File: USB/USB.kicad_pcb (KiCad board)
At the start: 4 copper layers, 70 x 60 mm, 20 parts, among them J1 USBC-4-0-CX90MW9-24P1, U2 ESDA25L, U3 USB SWITCH 2CHANNEL TS3USB221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, U6 usb-polarity-TUSB321RWBR

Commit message: added TVS protection and filtering to CC lines
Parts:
- added TVS4: ~, SPIRIT-footprints:1-channel-TVS-choke-XDFN6_1P2X1P2_ONS, F.Cu at (116.6, 82.4)
- moved J2 0.60 mm to (111.9, 83.7)
- moved J3 0.53 mm to (109.4, 83.7)
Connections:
- J1 pad A1: GND -> Net-(J1-GND_A)
- J1 pad A12: GND -> Net-(J1-GND_A)
- J2 pad 1: CC1 -> CC1f
- J2 pad 2: Net-(U6-CC1) -> CC1f-jumpered
- J3 pad 1: CC2 -> CC2f
- J3 pad 2: Net-(U6-CC2) -> CC2f-jumpered
- Module1 pad 94: CC1 -> CC1f-jumpered
- Module1 pad 96: CC2 -> CC2f-jumpered
- U6 pad 1: Net-(U6-CC1) -> CC1f-jumpered
- U6 pad 2: Net-(U6-CC2) -> CC2f-jumpered
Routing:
- net CC1f-jumpered: track 0.00 -> 57.0 mm, vias 0 -> 2
- net CC2f-jumpered: track 0.00 -> 56.3 mm, vias 0 -> 2
- net CC2: track 25.8 -> 16.8 mm
- net Net-(U6-CC1): track 8.32 -> 0.00 mm
- net Net-(U6-CC2): track 8.21 -> 0.00 mm
- net CC2f: track 0.00 -> 7.82 mm
- net CC1f: track 0.00 -> 4.58 mm
- net CC1: track 16.5 -> 12.7 mm

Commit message: fix TVS protection on CC lines
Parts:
- removed TVS4: ~, SPIRIT-footprints:1-channel-TVS-choke-XDFN6_1P2X1P2_ONS
- added D1: TPD1E05U06DPYR, CM5IO:TPD1E05U-SON65P60X100X45-2N, F.Cu at (120.8, 87.0)
- added D2: TPD1E05U06DPYR, CM5IO:TPD1E05U-SON65P60X100X45-2N, F.Cu at (122.8, 85.6)
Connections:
- net CC1f-jumpered renamed CC1-jumpered
- J2 pad 1: CC1f -> CC1
- J3 pad 1: CC2f -> CC2
- J3 pad 2: CC2f-jumpered -> CC2-jumpered
- Module1 pad 96: CC2f-jumpered -> CC2n-jumpered
- U6 pad 2: CC2f-jumpered -> CC2-jumpered
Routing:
- net CC2f-jumpered: track 56.3 -> 0.00 mm, vias 2 -> 0
- net (no net): track 0.00 -> 56.3 mm, vias 0 -> 2
- net CC2: track 16.8 -> 25.5 mm
- net CC2f: track 7.82 -> 0.00 mm
- net CC1f: track 4.58 -> 0.00 mm
- net CC1: track 12.7 -> 17.3 mm

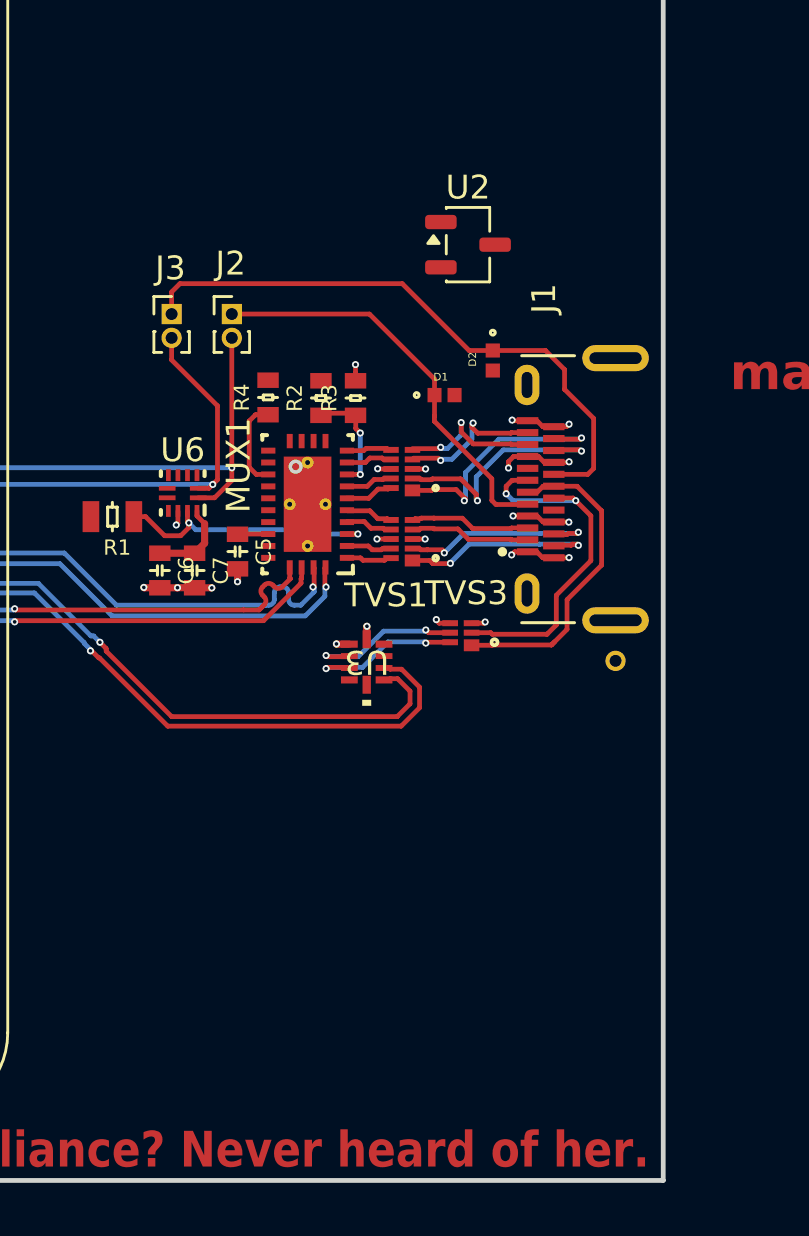
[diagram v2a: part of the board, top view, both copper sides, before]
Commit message: add lab power input headers
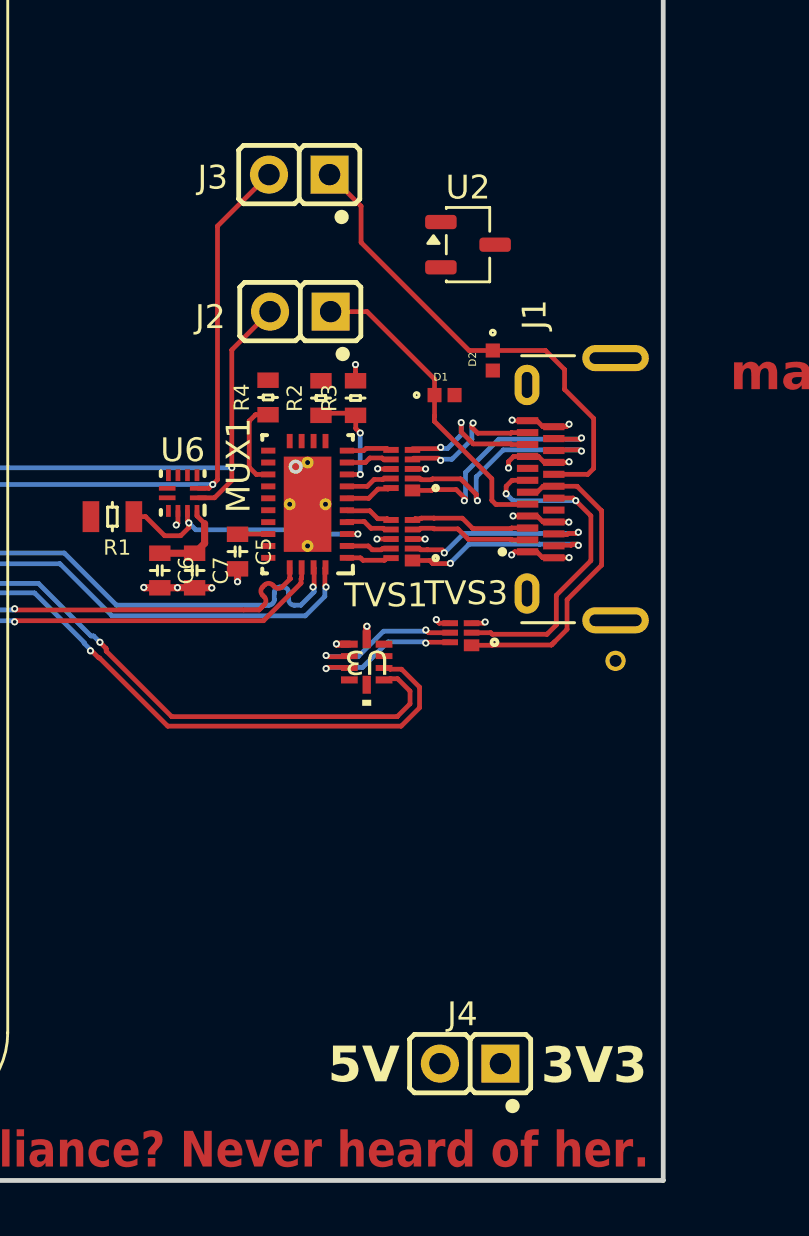
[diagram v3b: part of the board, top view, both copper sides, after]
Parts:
- added J4: ~, COMATEL THD:COMATEL_385.0358.1.02.400, F.Cu at (123.2, 115.1)
- J2, J3: footprint Connector_PinHeader_1.00mm:PinHeader_1x02_P1.00mm_Vertical -> COMATEL THD:COMATEL_385.0358.1.02.400
- moved J3 8.84 mm to (116.0, 77.8), turned to 180 degrees
- moved J2 4.15 mm to (116.0, 83.5), turned to 180 degrees
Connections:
- Module1 pad 96: CC2n-jumpered -> CC2-jumpered
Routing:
- net CC2-jumpered: track 0.00 -> 63.3 mm, vias 0 -> 2
- net (no net): track 56.3 -> 0.00 mm, vias 2 -> 0
- net CC2: track 25.5 -> 20.6 mm
- net CC1: track 17.3 -> 13.2 mm
- net CC1-jumpered: track 57.0 -> 58.8 mm
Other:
- board text added: "3V3"
- board text added: "5V"

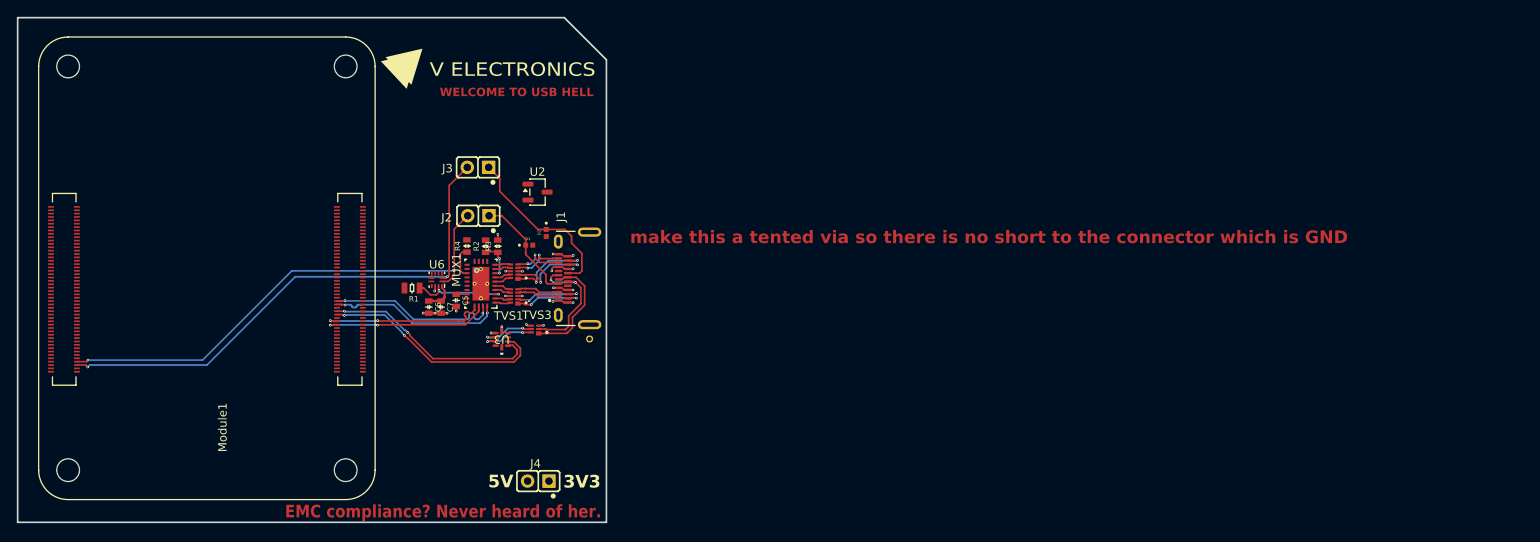
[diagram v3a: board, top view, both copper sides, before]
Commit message: add copper pours
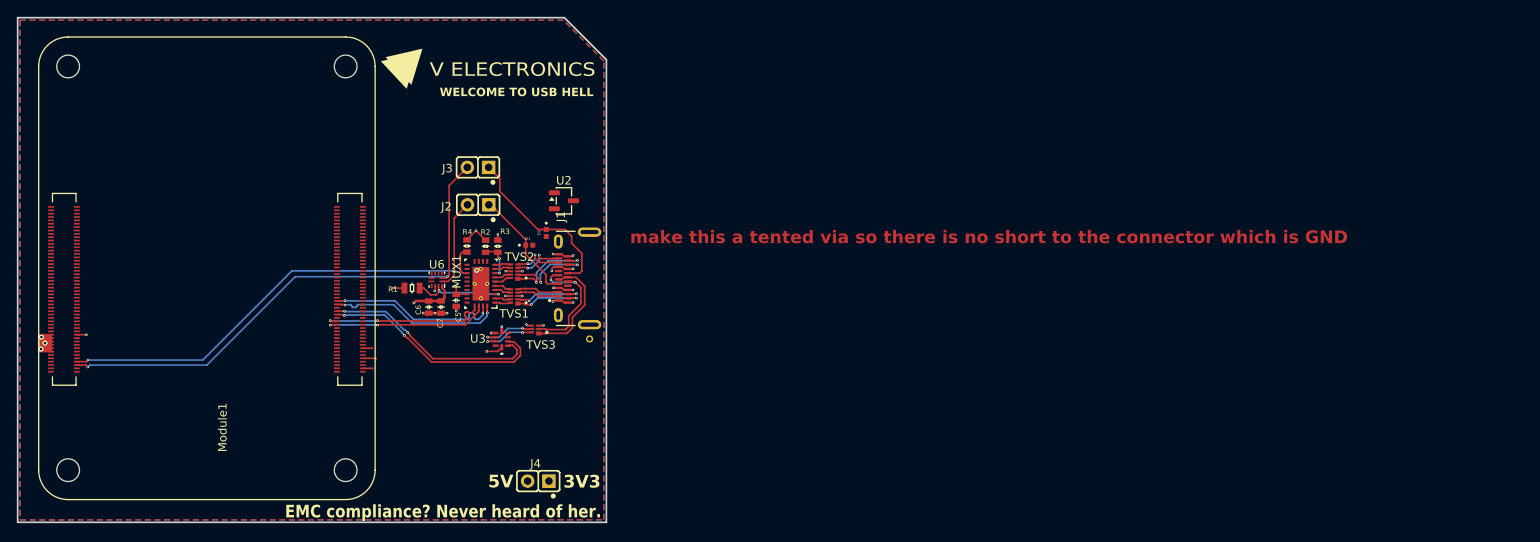
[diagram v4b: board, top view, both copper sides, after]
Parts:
- moved U2 3.31 mm to (125.0, 81.8)
- moved J2 1.30 mm to (116.0, 82.2)
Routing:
- net 3V3B: track 1.29 -> 9.87 mm, vias 0 -> 5
- net GND: track 14.4 -> 18.3 mm
- net 5V: track 3.54 -> 5.42 mm, vias 0 -> 4
- net CC1-jumpered: track 58.8 -> 60.1 mm
- net CC1: track 13.2 -> 13.8 mm
- added copper zone on In1.Cu, net 3V3B
- added copper zone on In2.Cu, net 5V
- added copper zone on B.Cu, net GND
- added copper zone on F.Cu, net GND

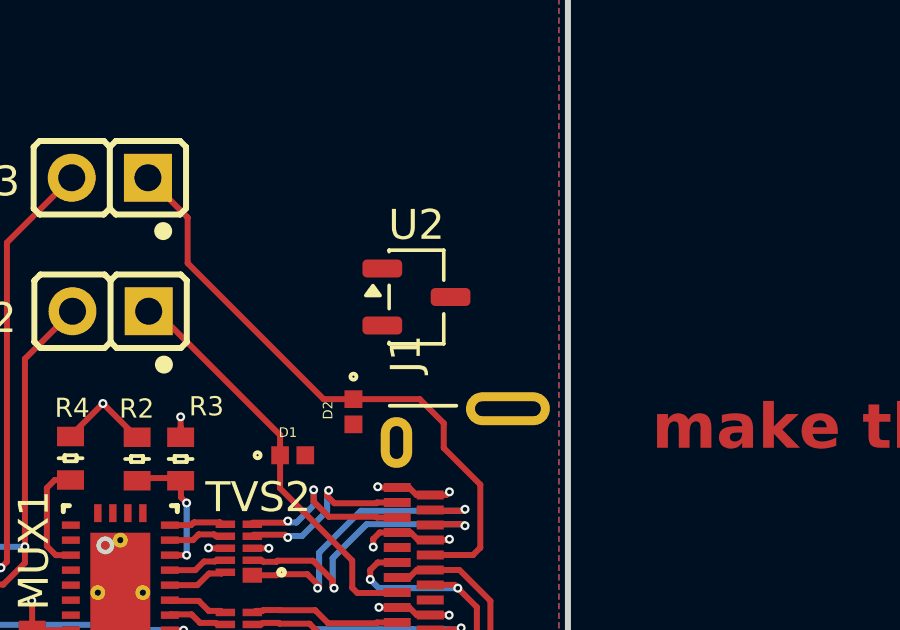
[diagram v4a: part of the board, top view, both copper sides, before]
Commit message: connect VBUS to 25V TVS and CC to CM5 for tests
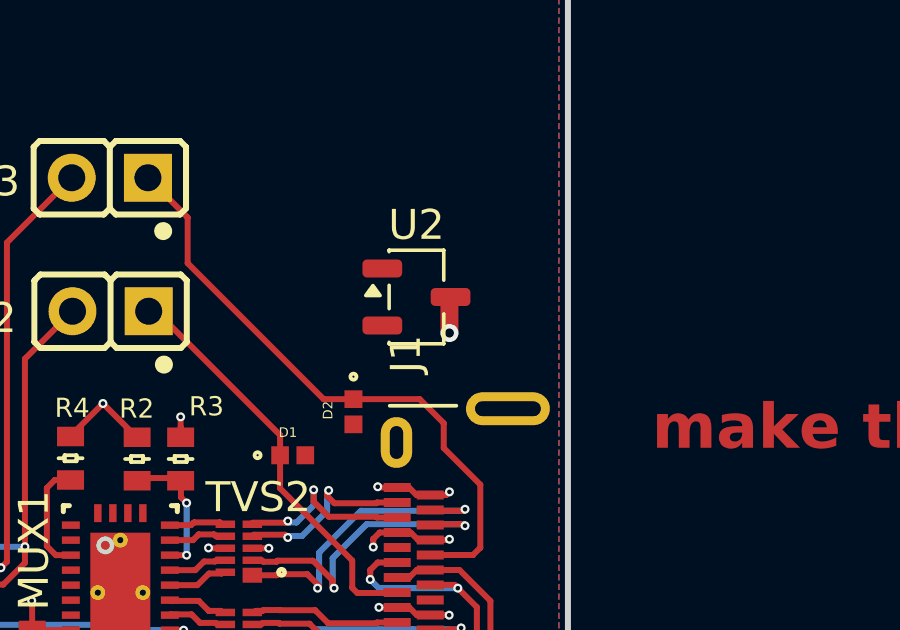
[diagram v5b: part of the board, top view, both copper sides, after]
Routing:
- net USBC POW: track 5.46 -> 23.6 mm, vias 4 -> 5

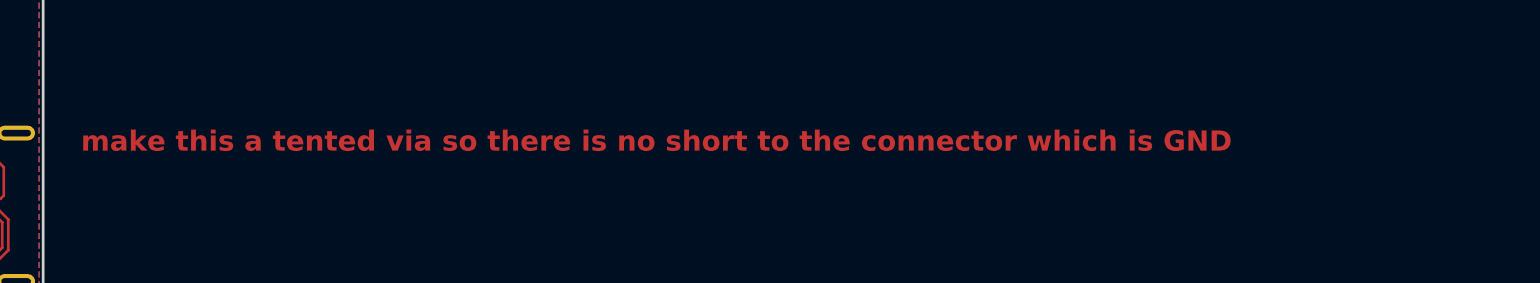
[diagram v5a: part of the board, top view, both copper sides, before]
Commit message: make vias under type c socket tented and add fab note
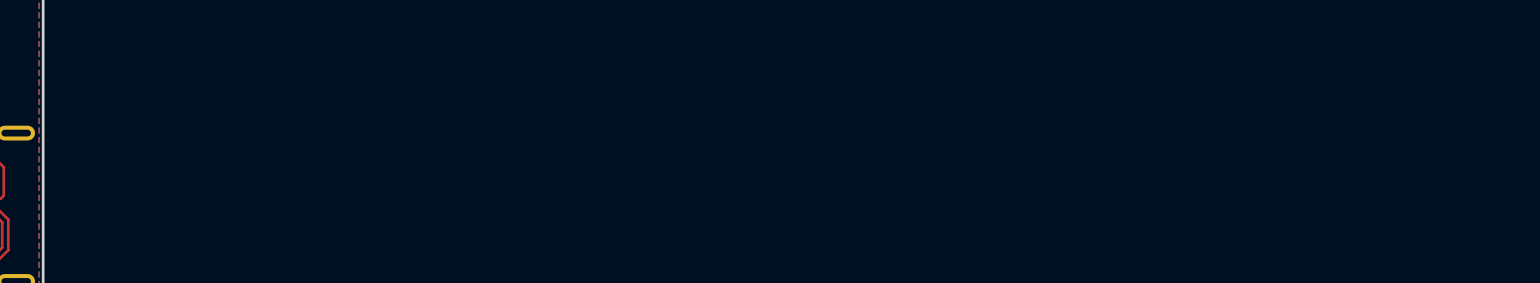
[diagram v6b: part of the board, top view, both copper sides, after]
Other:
- board text added: "note: vias under type C socket need to be tented from the top"
- board text removed: "make this a tented via so there is no short to the connector which is GND"
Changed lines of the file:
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@@
 		(layer "Edge.Cuts")
 	)
-	(gr_text "make this a tented via so there is no short to the connector which is GND\n\n"
-		(at 132.8 89.4 0)
-		(layer "F.Cu")
-		(effects
-			(font
-				(size 1.5 1.5)
-				(thickness 0.3)
-				(bold yes)
-			)
-			(justify left bottom)
-		)
-	)
 	(gr_text "WELCOME TO USB HELL"
 		(at 110.175 69.45 0)
@@
 		)
 	)
+	(gr_text "note: vias under type C socket\nneed to be tented from the top"
+		(at 132.8 89.4 0)
+		(layer "F.Fab")
+		(effects
+			(font
+				(size 1.5 1.5)
+				(thickness 0.3)
+				(bold yes)
+			)
+			(justify left bottom)
+		)
+	)
 	(segment
 		(start 120.4 88.15)
@@
 		(drill 0.15)
 		(layers "F.Cu" "B.Cu")
+		(tenting
+			(front yes)
+			(back no)
+		)
 		(capping no)
 		(covering
@@
 		(drill 0.15)
 		(layers "F.Cu" "B.Cu")
+		(tenting
+			(front yes)
+			(back no)
+		)
 		(capping no)
 		(covering
@@
 		(drill 0.15)
 		(layers "F.Cu" "B.Cu")
+		(tenting
+			(front yes)
+			(back no)
+		)
 		(capping no)
 		(covering
@@
 		(drill 0.15)
 		(layers "F.Cu" "B.Cu")
+		(tenting
+			(front yes)
+			(back no)
+		)
 		(capping no)
 		(covering
@@
 		(drill 0.15)
 		(layers "F.Cu" "B.Cu")
+		(tenting
+			(front yes)
+			(back no)
+		)
 		(capping no)
 		(covering
@@
 		(drill 0.15)
 		(layers "F.Cu" "B.Cu")
+		(tenting
+			(front yes)
+			(back no)
+		)
 		(capping no)
 		(covering
@@
 		(drill 0.15)
 		(layers "F.Cu" "B.Cu")
+		(tenting
+			(front yes)
+			(back no)
+		)
 		(capping no)
 		(covering
@@
 		(drill 0.15)
 		(layers "F.Cu" "B.Cu")
+		(tenting
+			(front yes)
+			(back no)
+		)
 		(capping no)
 		(covering
@@
 		(drill 0.15)
 		(layers "F.Cu" "B.Cu")
+		(tenting
+			(front yes)
+			(back no)
+		)
 		(capping no)
 		(covering
@@
 		(drill 0.15)
 		(layers "F.Cu" "B.Cu")
+		(tenting
+			(front yes)
+			(back no)
+		)
 		(capping no)
 		(covering
@@
 		(drill 0.15)
 		(layers "F.Cu" "B.Cu")
+		(tenting
+			(front yes)
+			(back no)
+		)
 		(capping no)
 		(covering
@@
 		(drill 0.15)
 		(layers "F.Cu" "B.Cu")
+		(tenting
+			(front yes)
+			(back no)
+		)
 		(capping no)
 		(covering
@@
 		(drill 0.15)
 		(layers "F.Cu" "B.Cu")
+		(tenting
+			(front yes)
+			(back no)
+		)
 		(capping no)
 		(covering
@@
 		(drill 0.15)
 		(layers "F.Cu" "B.Cu")
+		(tenting
+			(front yes)
+			(back no)
+		)
 		(capping no)
 		(covering

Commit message: add test points for USB SWITCH and MUX POL
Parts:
- added J5: ~, COMATEL THD:COMATEL_385.0358.1.02.400, F.Cu at (123.3, 109.5)
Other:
- board text added: "MUX POL"
- board text added: "USB SWITCH"

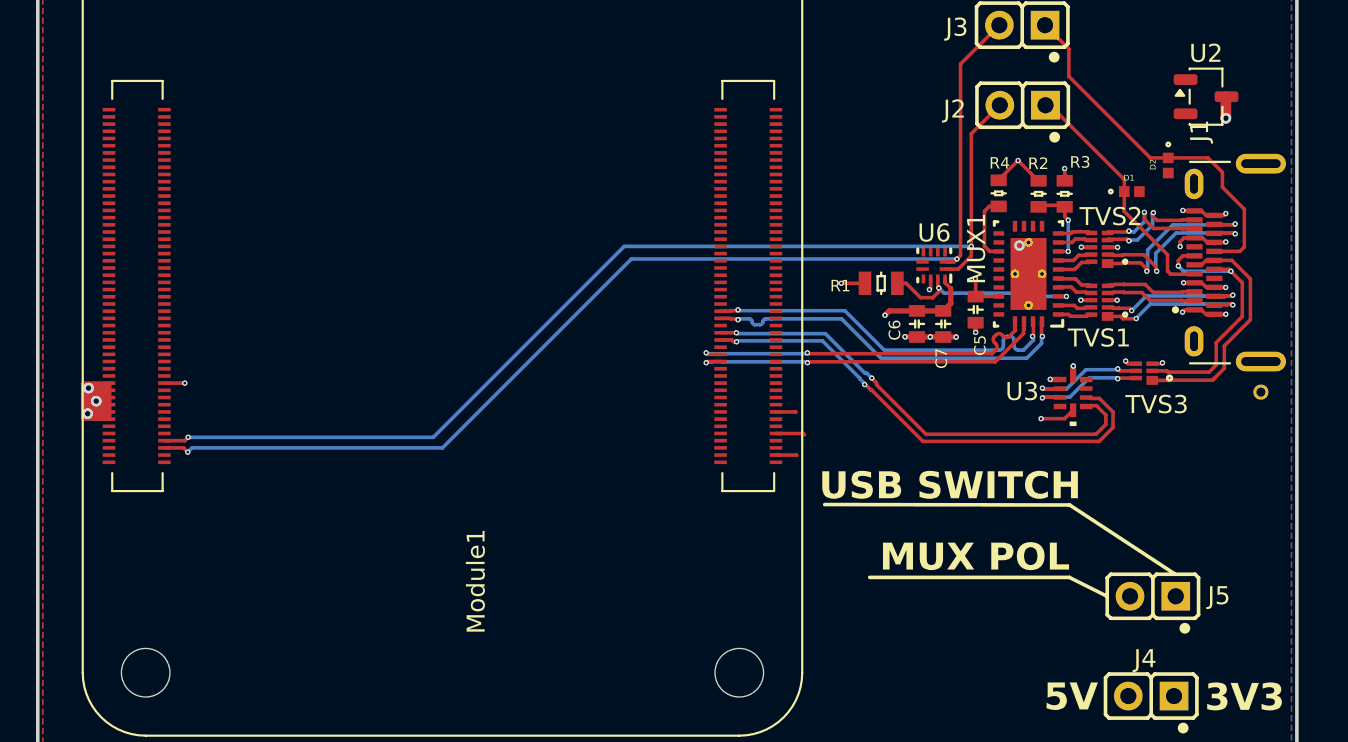
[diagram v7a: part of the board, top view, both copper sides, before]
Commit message: connect test points and connect CM5 to plane
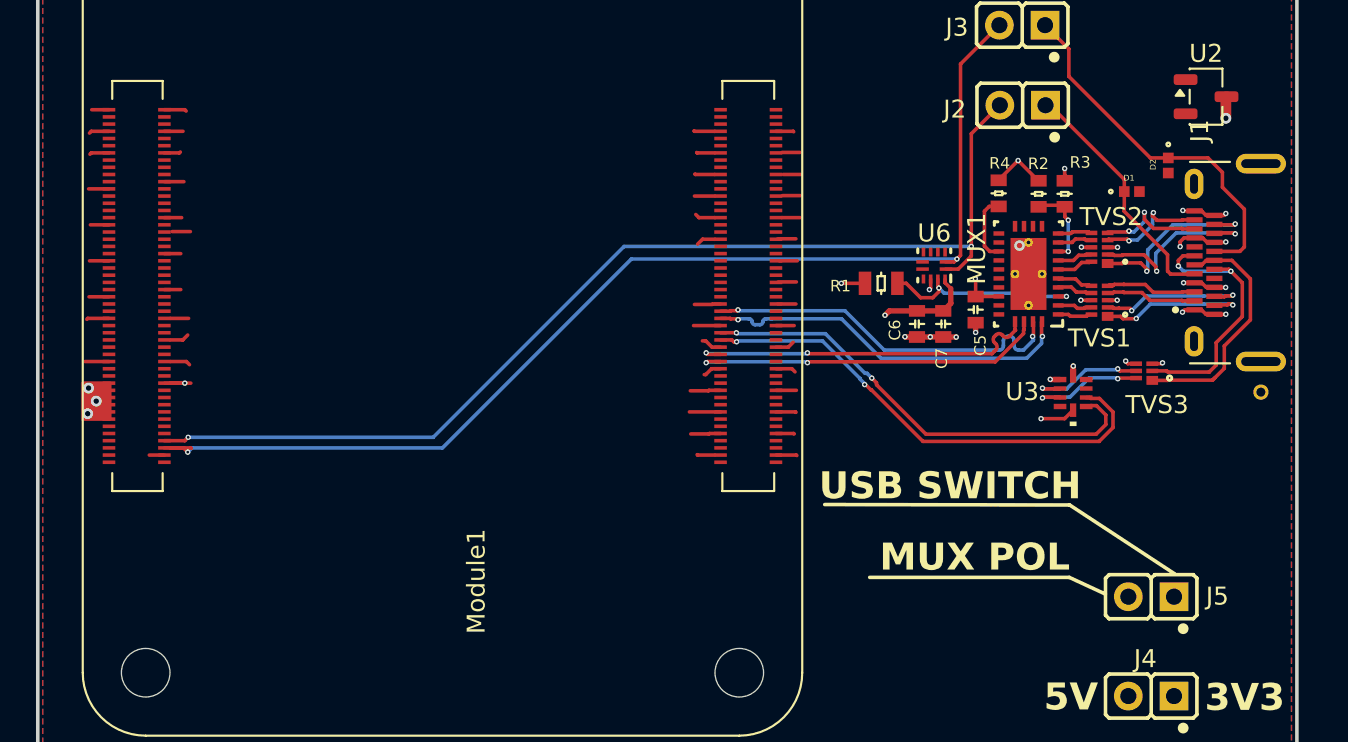
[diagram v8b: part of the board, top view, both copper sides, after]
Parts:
- moved J5 0.10 mm to (123.2, 109.6)
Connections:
- Module1 pad 59: unconnected-(Module1A-GND-Pad59) -> GND
- Module1 pad 7: unconnected-(Module1A-GND-Pad7) -> GND
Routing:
- net GND: track 18.3 -> 69.1 mm
- net CC2-jumpered: track 63.3 -> 64.4 mm
- net 3V3B: track 9.87 -> 11.0 mm
- net unconnected-(Module1A-SD_DAT6-Pad72): track 0.00 -> 1.13 mm
- net unconnected-(Module1A-ID_SD-Pad36): track 0.00 -> 1.01 mm
